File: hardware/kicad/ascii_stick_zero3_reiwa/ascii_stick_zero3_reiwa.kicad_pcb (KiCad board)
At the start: 2 copper layers, 20 parts, among them J1 USB_B_Micro, J2 Buttons_1, J3 AVR-ISP-6, J4 Buttons_2, J5 Buttons_3, J6 Buttons_4, J7 STICK, J8 STICK_POWER, U1 ATmega32U4-A, Y1 Crystal

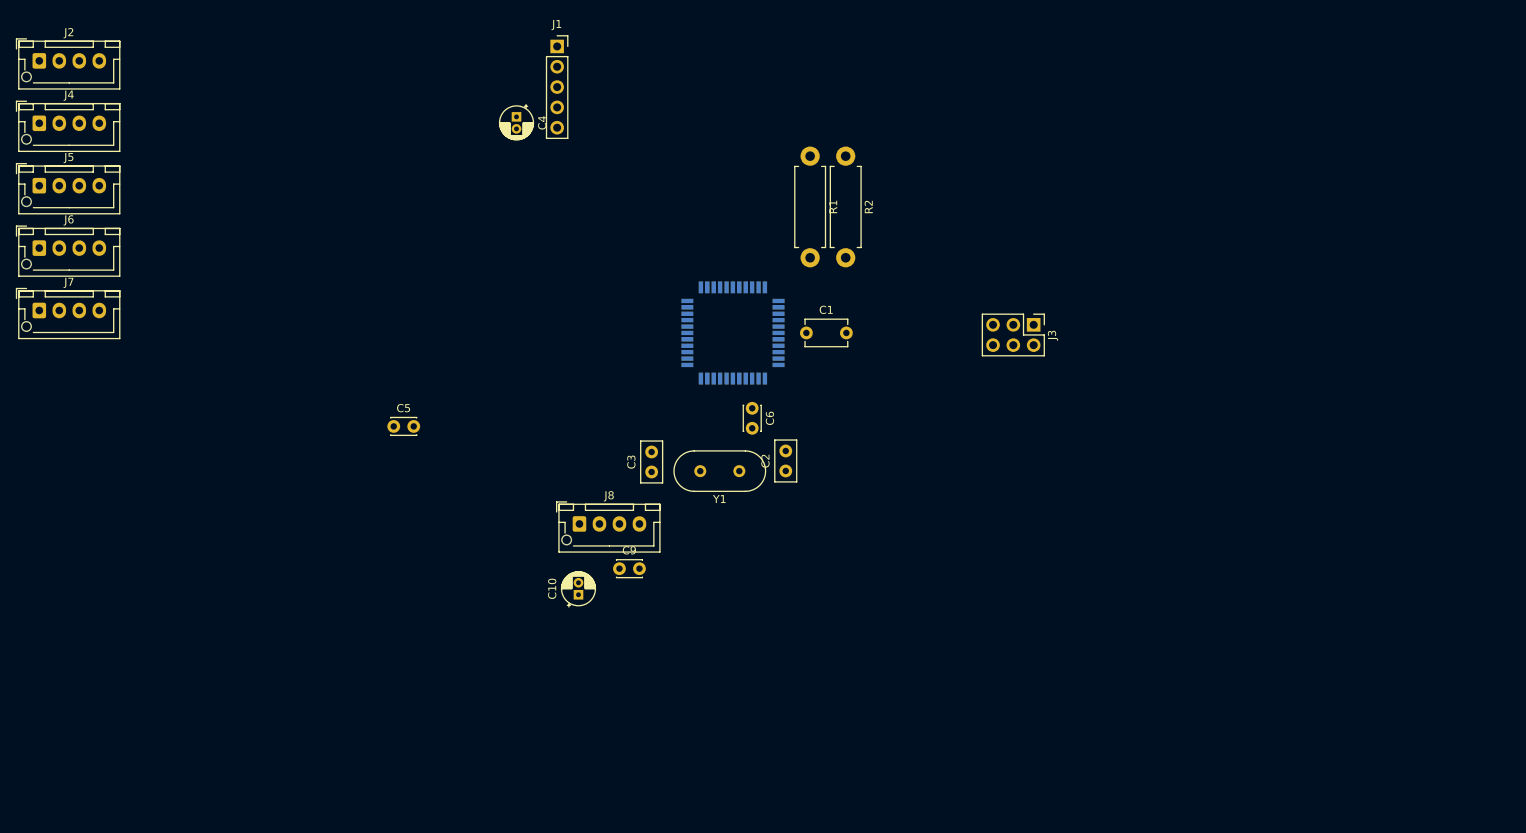
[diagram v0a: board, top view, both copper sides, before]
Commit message: for hand-etching
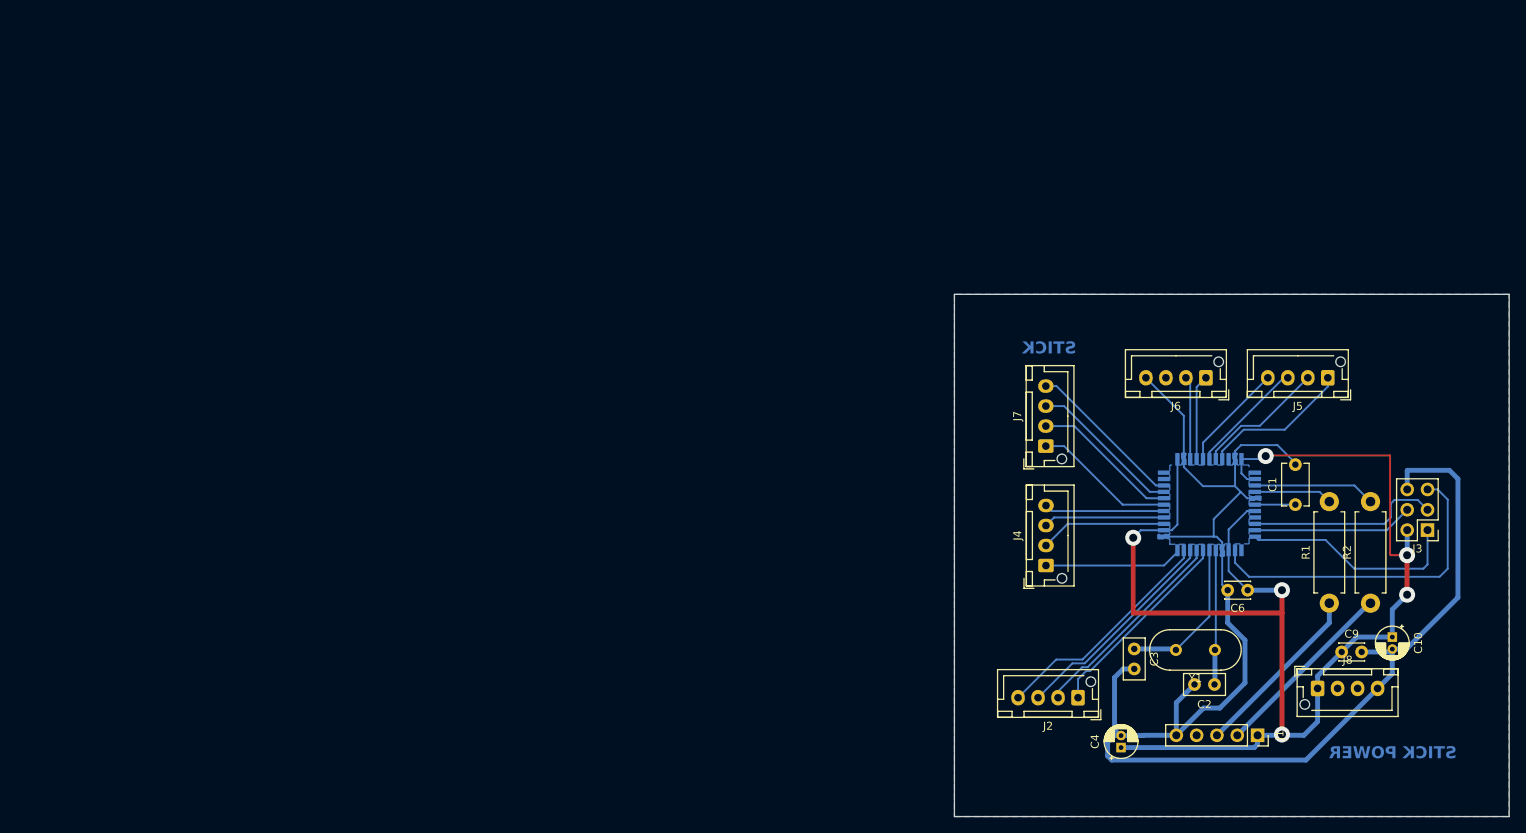
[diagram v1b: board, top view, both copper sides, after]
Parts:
- removed C5: 0.1u, Capacitor_THT:C_Disc_D3.0mm_W2.0mm_P2.50mm
- moved J5 162.8 mm to (209.0, 76.2), turned to 180 degrees
- moved J2 152.3 mm to (177.8, 116.2), turned to 180 degrees
- moved J6 146.7 mm to (193.7, 76.2), turned to 180 degrees
- moved J4 137.4 mm to (173.8, 99.7), turned to 90 degrees
- moved J7 127.0 mm to (173.7, 84.8), turned to 90 degrees
- moved J1 122.8 mm to (200.2, 120.9), turned to -90 degrees
- moved C4 109.2 mm to (183.1, 122.4), turned to 90 degrees
- moved C10 101.9 mm to (217.0, 108.6), turned to -90 degrees
- moved J8 94.5 mm to (207.7, 115.0)
- moved C9 90.9 mm to (210.7, 110.5)
- moved R2 86.2 mm to (214.3, 104.4), turned to 90 degrees
- moved R1 85.6 mm to (209.2, 104.4), turned to 90 degrees
- moved C6 66.0 mm to (199.0, 102.8), turned to 180 degrees
- moved C1 64.8 mm to (204.9, 92.1), turned to 90 degrees
- moved C3 64.3 mm to (184.8, 110.1), turned to -90 degrees
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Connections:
- U1 pad 12: /RIGHT -> unconnected-(U1-PB7-Pad12)
- U1 pad 22: /BUTTON5 -> /BUTTON4
- U1 pad 25: /BUTTON4 -> /BUTTON5
- U1 pad 31: unconnected-(U1-PC6-Pad31) -> /RIGHT
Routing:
- net GND: track 0.00 -> 192.3 mm
- net VCC: track 0.00 -> 172.5 mm, vias 0 -> 6
- net Net-(J3-~{RST}): track 0.00 -> 41.0 mm
- net /BUTTON3: track 0.00 -> 28.9 mm
- net Net-(J3-MISO): track 0.00 -> 27.7 mm
- net /BUTTON2: track 0.00 -> 27.2 mm
- net /BUTTON1: track 0.00 -> 26.0 mm
- net /BUTTON0: track 0.00 -> 25.2 mm
- net Net-(J3-SCK): track 0.00 -> 24.3 mm
- net Net-(J1-D-): track 0.00 -> 23.5 mm
- net Net-(J1-D+): track 0.00 -> 22.3 mm
- net Net-(J3-MOSI): track 0.00 -> 20.1 mm
- net /RIGHT: track 0.00 -> 19.9 mm
- net Net-(U1-XTAL1): track 0.00 -> 19.5 mm
- net /LEFT: track 0.00 -> 19.2 mm
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- added copper zone on B.Cu, net GND
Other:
- board outline added: 69.3 x 65.3 mm
- board text added: "STICK"
- board text added: "STICK POWER"

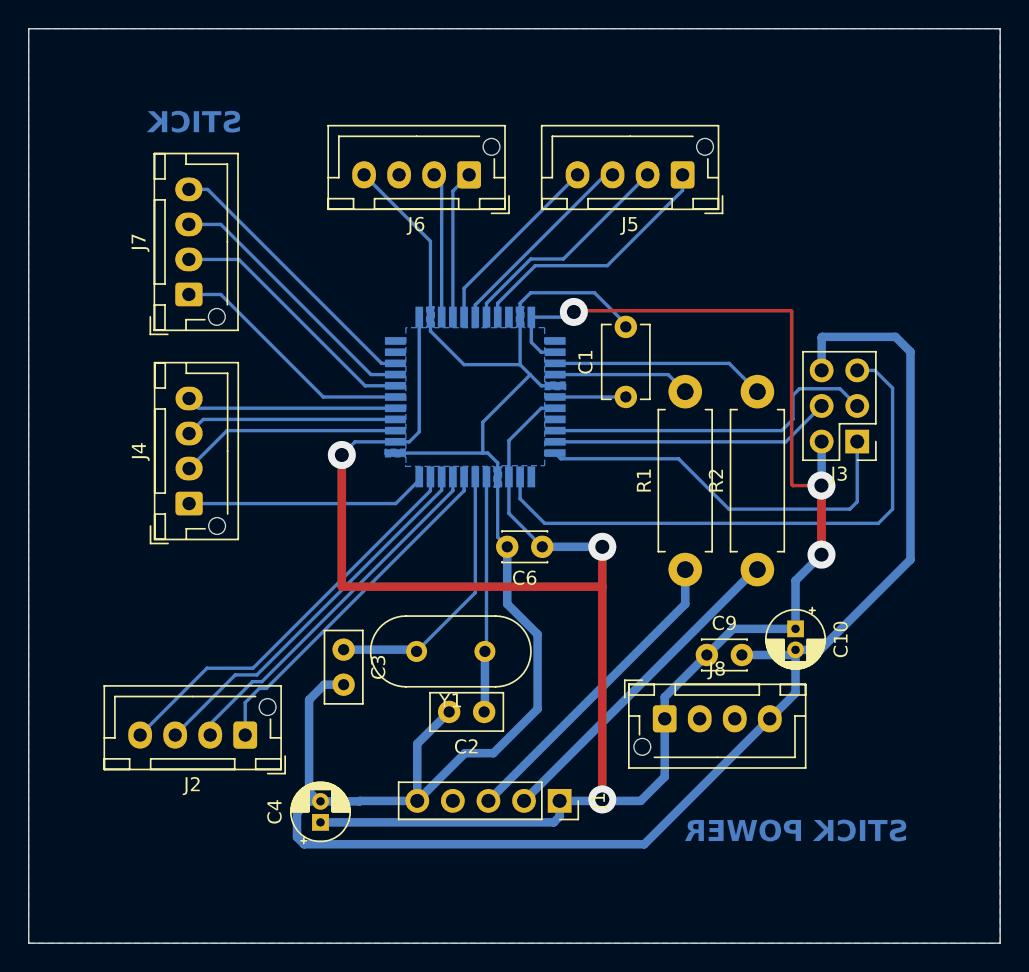
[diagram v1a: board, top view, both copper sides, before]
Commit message: follow jlcpcb constraints
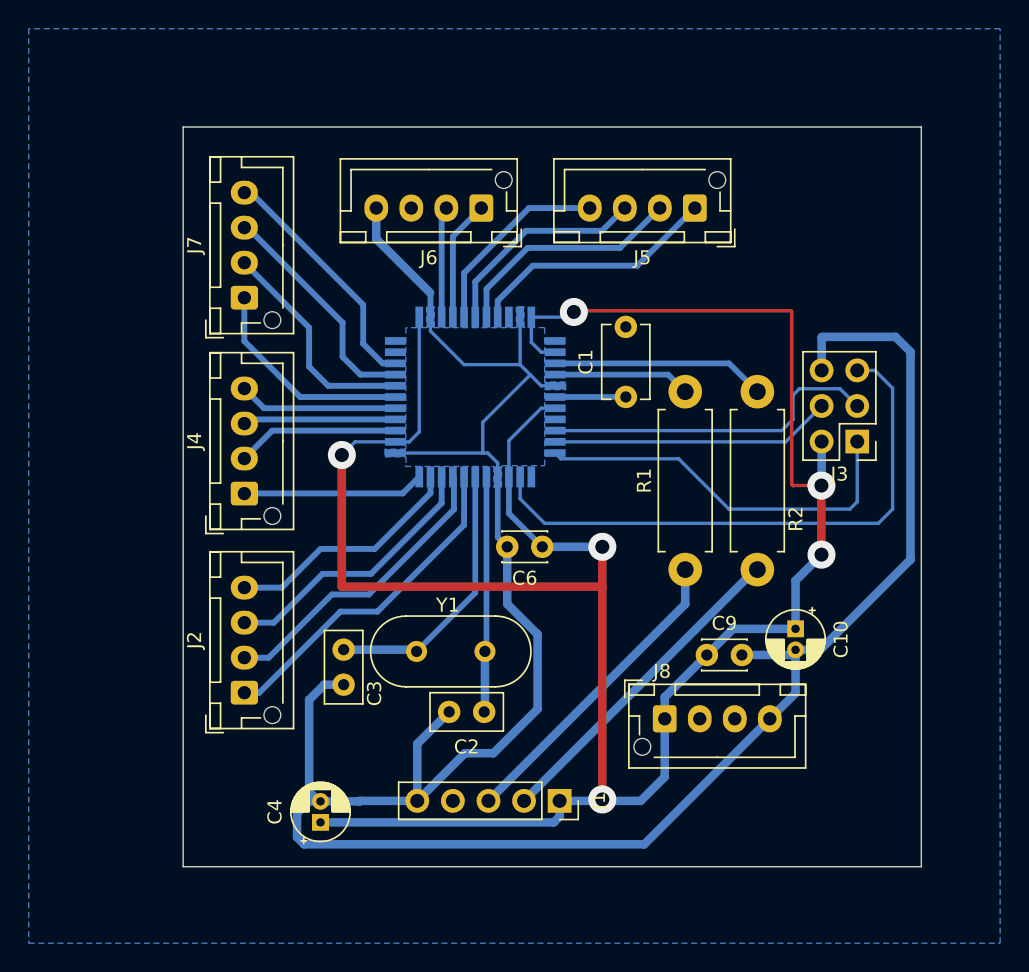
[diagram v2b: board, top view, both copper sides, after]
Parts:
- moved J4 4.01 mm to (177.7, 99.0)
- moved J7 3.97 mm to (177.7, 85.0)
- moved J2 3.02 mm to (177.7, 113.2), turned to 90 degrees
- moved J5 2.53 mm to (209.9, 78.6)
- moved J6 2.53 mm to (194.6, 78.6)
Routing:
- net GND: track 192.3 -> 179.6 mm
- net /BUTTON3: track 28.9 -> 17.2 mm
- net /BUTTON2: track 27.2 -> 19.5 mm
- net /BUTTON4: track 17.4 -> 13.0 mm
- net /BUTTON1: track 26.0 -> 21.7 mm
- net /BUTTON6: track 15.1 -> 10.9 mm
- net /BUTTON5: track 15.9 -> 11.6 mm
- net /BUTTON7: track 15.0 -> 11.4 mm
- net /LEFT: track 19.2 -> 16.6 mm
- net /BUTTON13: track 10.4 -> 7.92 mm
- net /RIGHT: track 19.9 -> 17.5 mm
- net /DOWN: track 18.5 -> 16.1 mm
- net /UP: track 17.8 -> 15.5 mm
- net /BUTTON12: track 10.6 -> 8.63 mm
- net /BUTTON0: track 25.2 -> 24.1 mm
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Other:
- board size 69.3 x 65.3 mm -> 52.7 x 52.8 mm
- board text removed: "STICK"
- board text removed: "STICK POWER"
